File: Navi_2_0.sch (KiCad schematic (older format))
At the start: 108 parts, among them J1 USB_B_Micro, J10 BAT-, J2 Conn_01x24_Male, J23 Conn_01x06_Male, J27 Micro_SD_Card_Det, J8 SELECT, J9 BAT+, Q1 DMG2301L-7, Q2 TF2310, Q3 DMG2301L-7, Q6 DMG2301L-7, SW1 SW_Push, SW2 SW_Push, U1 MT3420C, U2 MT3420C, U3 ESP32-WROOM-32, U4 CH330N, U5 L96-M33, U6 LSM6DS3, U7 TCN75-3.3

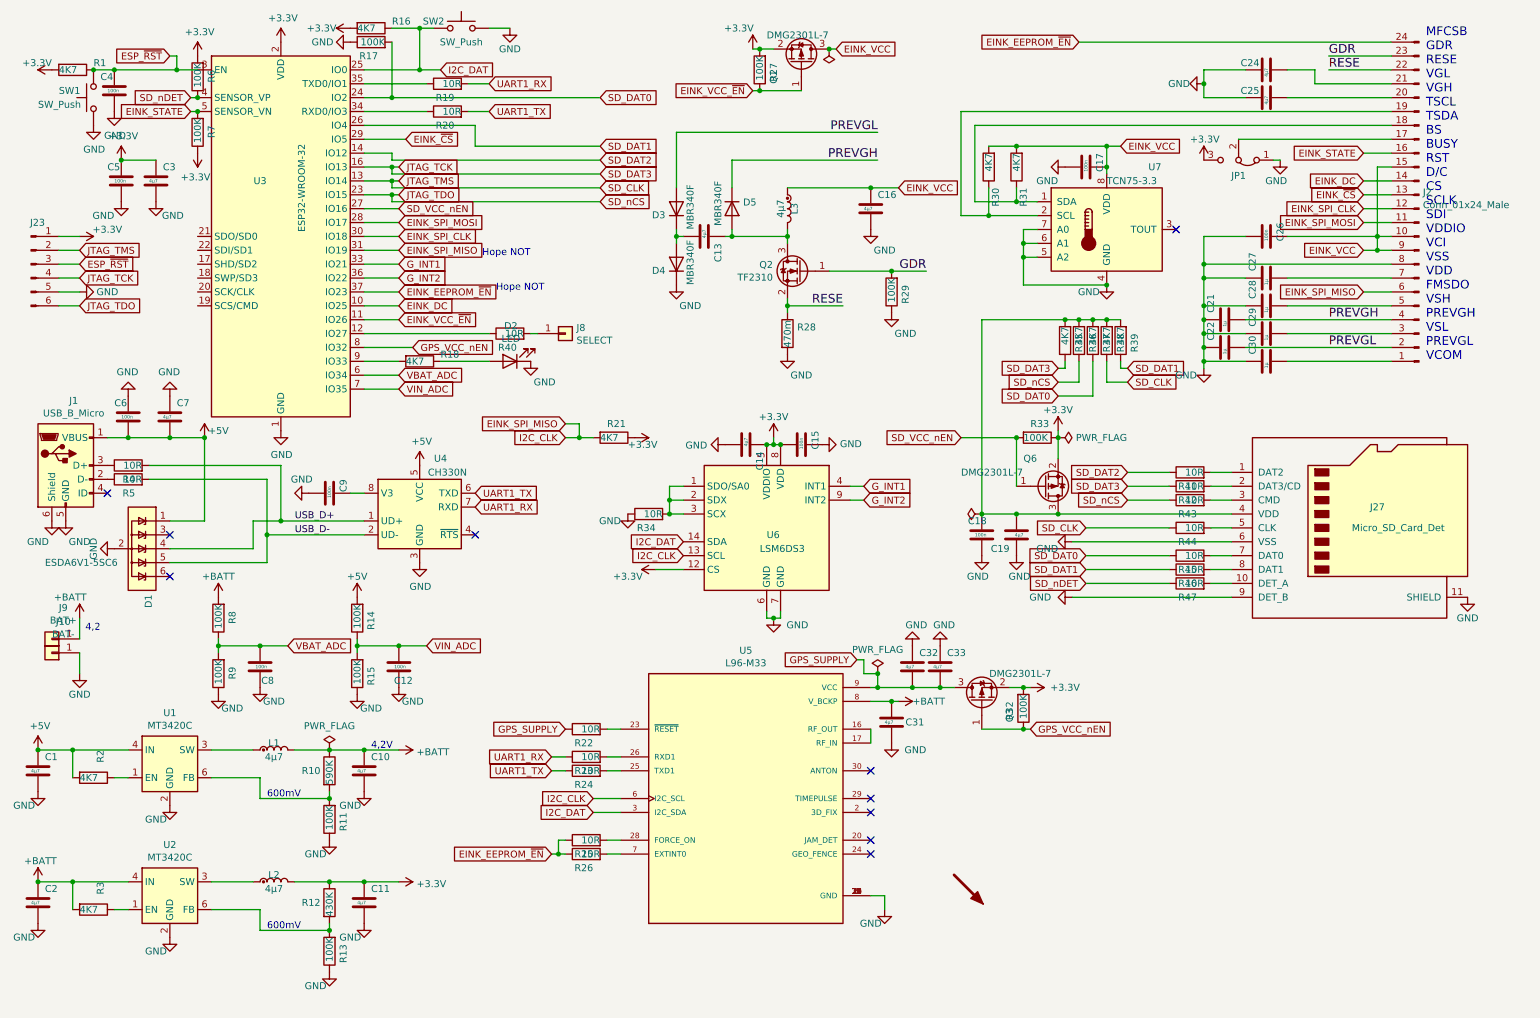
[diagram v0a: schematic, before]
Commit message: Again PullUP Widerstand SD Karte
#4 zum zweitenmal den Pull Up Widerstand ergänzt
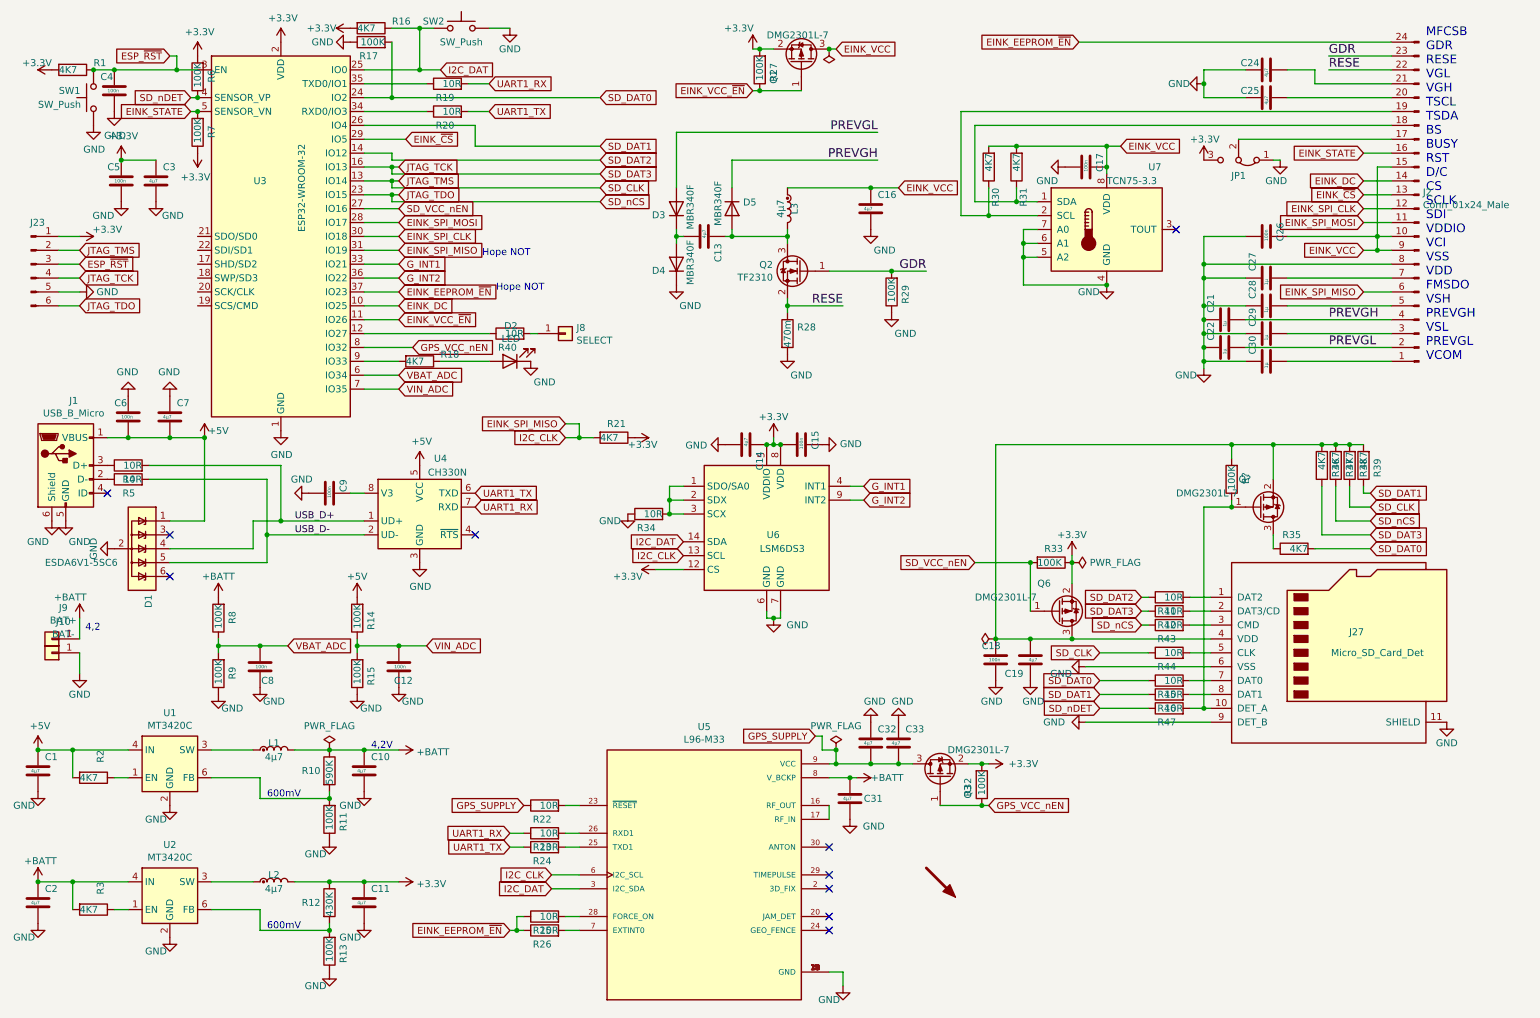
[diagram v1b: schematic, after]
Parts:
- added Q?: DMG2301L-7, Package_TO_SOT_SMD:TSOT-23, symbol Device:Q_PMOS_GSD
- added R?: 100K, Resistor_SMD:R_0603_1608Metric, symbol Device:R
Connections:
- net JTAG_TCK: now also R36.1; no longer R35.1
- net JTAG_TDO: now also R37.1; no longer R36.1
- net SD_DAT0: now also R35.2; no longer R37.1
- net at C18.1, C19.2, J27.4 (VDD)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: now also Q?.2 (S), R?.2; no longer R35.2
- net at J27.10 (DET_A), R47.2: now also Q?.1 (G), R?.1
- new net: Q?.3 (D), R35.1
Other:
- moved on the sheet: C18, C19, C31, C32, C33, J27, Q3, Q6, R22, R23, R24, R25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
